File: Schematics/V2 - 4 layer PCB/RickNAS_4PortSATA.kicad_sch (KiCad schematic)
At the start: 39 parts, among them J1 2227595-1, J10 10076579-002C-TRLF, J3 Conn_01x03, J6 Molex 4-pin, J7 10076579-002C-TRLF, J8 10076579-002C-TRLF, J9 10076579-002C-TRLF, U1 CH32V003FxPx, U2 TLV1117-33

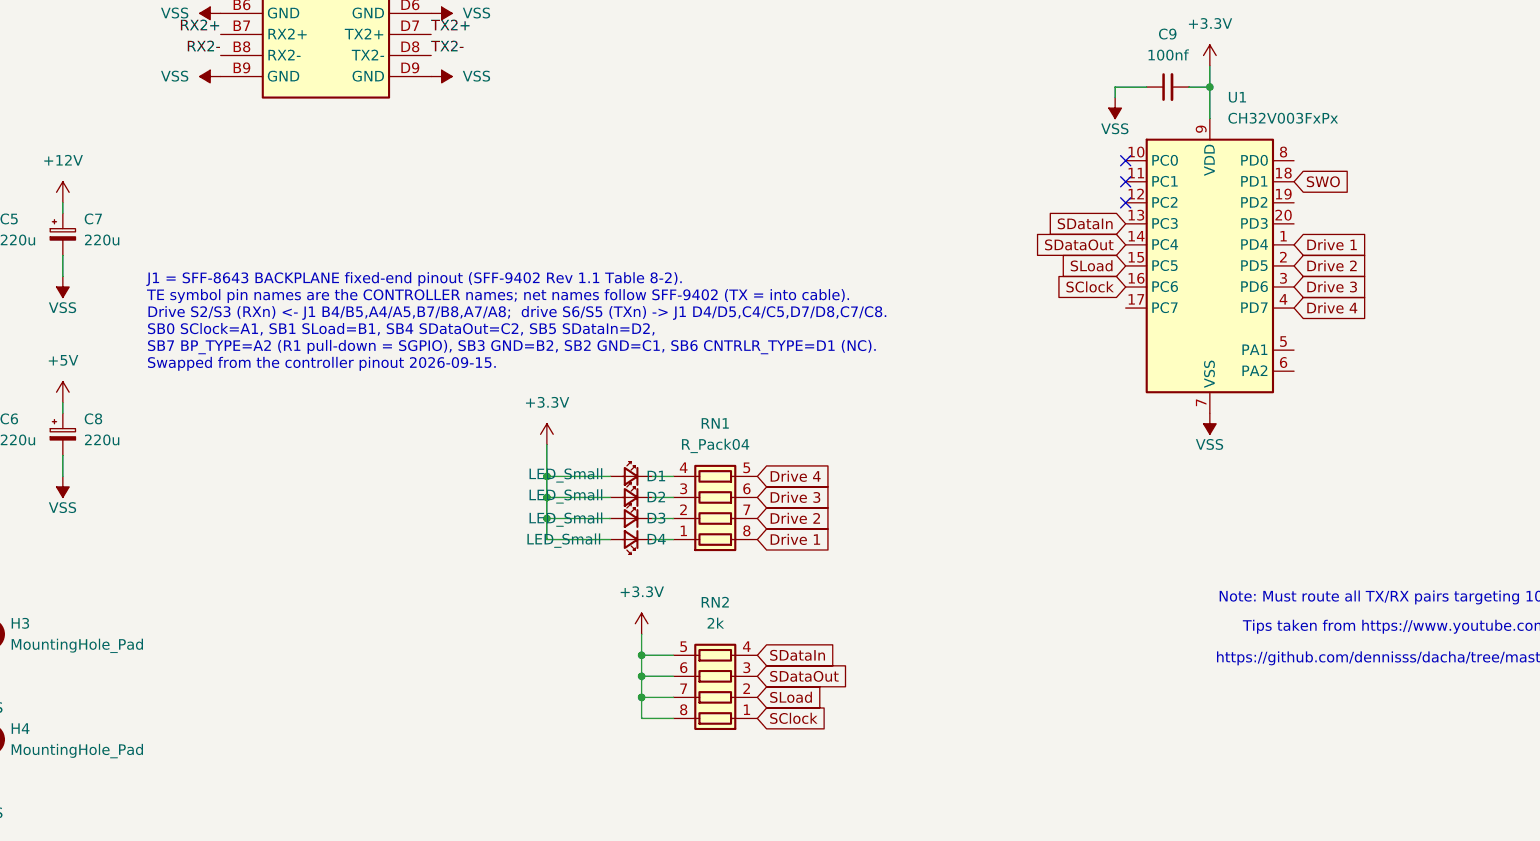
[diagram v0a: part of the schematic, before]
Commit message: Add per-bay fault/locate LEDs on spare CH32V003 pins
D5-D8 (red 0805) + RN3 1k array, wired like the activity LEDs D1-D4
(anode +3.3V, sunk through the array by U1). Global labels Fault 1-4:
  Fault 1 -> PC0 (pin 10), Fault 2 -> PC7 (17),
  Fault 3 -> PD0 (8),      Fault 4 -> PA1 (5)
Leaves PC1/PC2 (I2C) and PD2/PD3/PA2 (ADC) free. Each bay's fault LED
shares a row with its activity LED (Drive n / Fault n on the same
RN pair position). Firmware: SGPIO locate/fault bits drive these.

Co-Authored-By: Claude Opus 5 <noreply@anthropic.com>
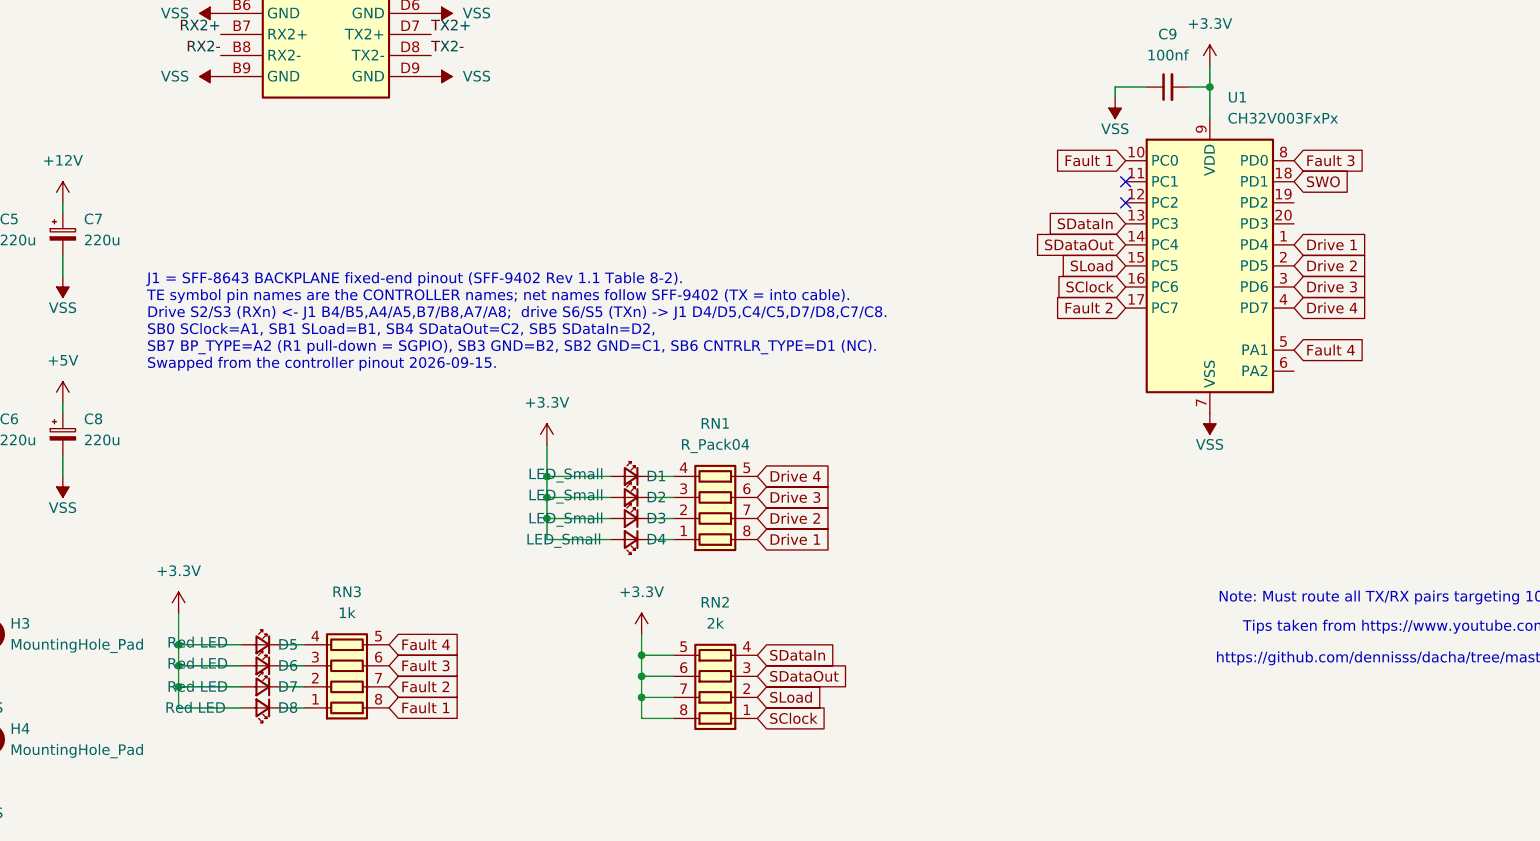
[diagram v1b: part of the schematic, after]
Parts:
- added D5, D6, D7, D8: Red LED, LED_SMD:LED_0805_2012Metric, symbol Device:LED_Small
- added RN3: 1k, Resistor_SMD:R_Array_Concave_4x0603, symbol Device:R_Pack04
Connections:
- net +3.3V: now also D5.2 (A), D6.2 (A), D7.2 (A), D8.2 (A)
- net Fault 1: now reaches U1.10 (PC0)
- net Fault 1: now also RN3.8 (R1.2)
- net Fault 2: now reaches U1.17 (PC7)
- net Fault 2: now also RN3.7 (R2.2)
- net Fault 4: now reaches U1.5 (PA1)
- net Fault 4: now also RN3.5 (R4.2)
- net Fault 3: now reaches U1.8 (PD0)
- net Fault 3: now also RN3.6 (R3.2)
- new net: D8.1 (K), RN3.1 (R1.1)
- new net: D7.1 (K), RN3.2 (R2.1)
- new net: D6.1 (K), RN3.3 (R3.1)
- new net: D5.1 (K), RN3.4 (R4.1)
- no-connect marks 24 -> 23

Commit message: Revert "Add per-bay fault/locate LEDs on spare CH32V003 pins"
This reverts commit eeb4463. William is adding the fault LEDs himself.

Co-Authored-By: Claude Opus 5 <noreply@anthropic.com>
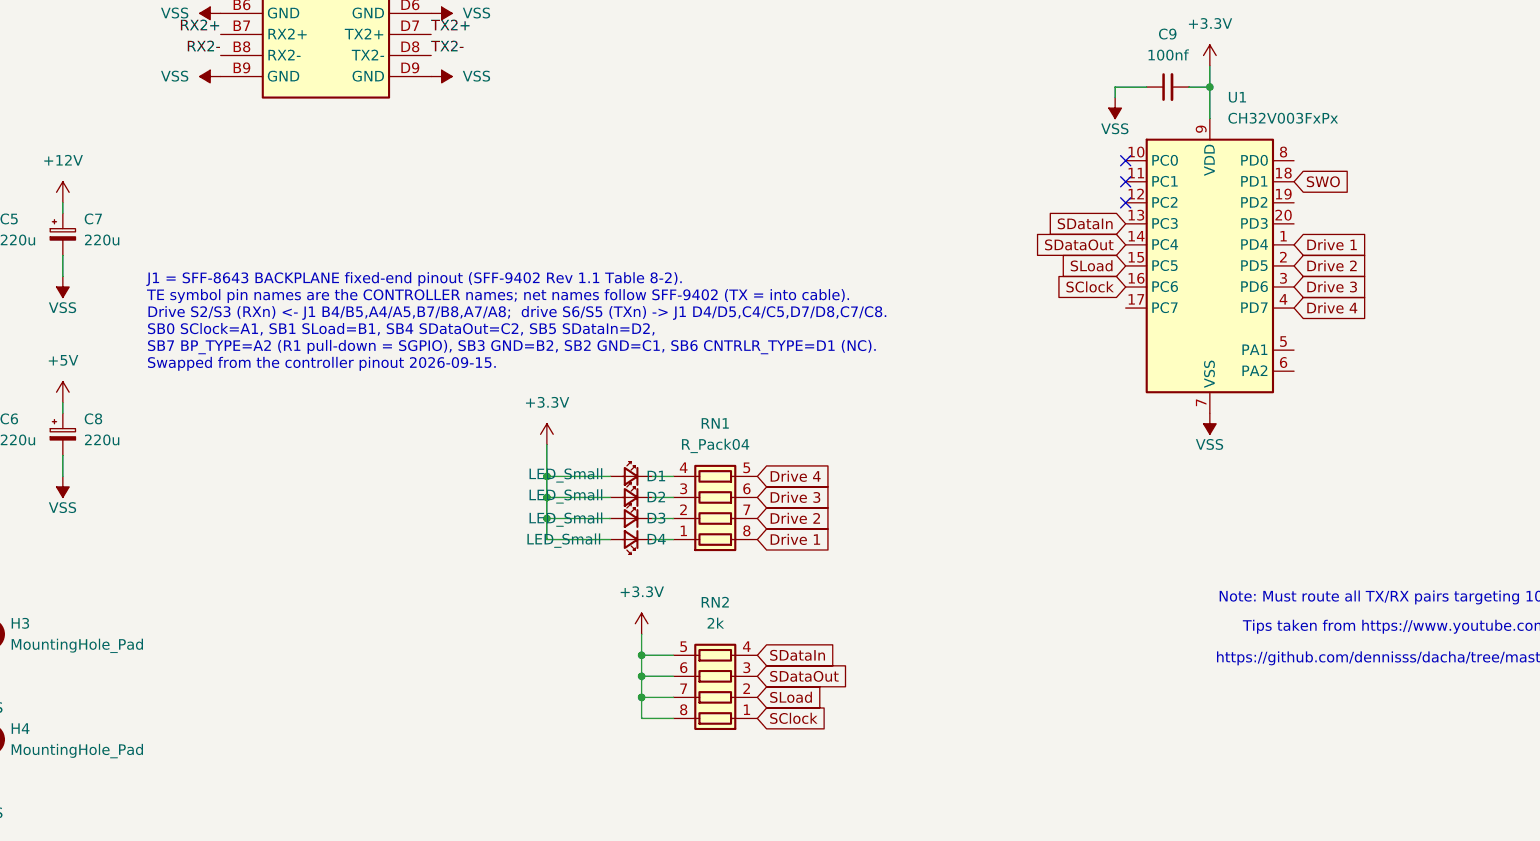
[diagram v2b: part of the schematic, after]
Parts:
- removed D5, D6, D7, D8: Red LED, LED_SMD:LED_0805_2012Metric, symbol Device:LED_Small
- removed RN3: 1k, Resistor_SMD:R_Array_Concave_4x0603, symbol Device:R_Pack04
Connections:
- net Fault 1: no longer names the net of U1.10 (PC0)
- net Fault 2: no longer names the net of U1.17 (PC7)
- net Fault 3: no longer names the net of U1.8 (PD0)
- net Fault 4: no longer names the net of U1.5 (PA1)
- no-connect marks 23 -> 24
